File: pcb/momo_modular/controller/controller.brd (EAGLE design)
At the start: 19 parts, among them U6 PIC24F16KA101-X_PSSOP, U7 FLASH8MSOP8

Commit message: Finished version 1 of the controller and wall_power boards.
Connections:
- removed net RX: U6.6
- removed net TX: U6.11
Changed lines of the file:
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@@
 <text x="31.877" y="40.9194" size="0.8128" layer="21">D</text>
 <text x="31.877" y="39.624" size="0.8128" layer="21">A</text>
-<dimension x1="55.88" y1="12.1158" x2="55.88" y2="42.6974" x3="58.8264" y3="27.4066" textsize="0.8128" layer="49" dtype="vertical" unit="inch" visible="yes"/>
 <wire x1="30.4292" y1="42.6466" x2="55.8292" y2="42.6466" width="0.254" layer="21"/>
 <wire x1="30.4292" y1="42.6466" x2="30.4292" y2="12.1666" width="0.254" layer="21"/>
 <wire x1="30.4292" y1="12.1666" x2="55.8292" y2="12.1666" width="0.254" layer="21"/>
-<dimension x1="30.4292" y1="42.6466" x2="55.88" y2="42.6974" x3="43.1546" y3="44.5262" textsize="0.8128" layer="21" dtype="horizontal" unit="inch" visible="yes"/>
+<dimension x1="30.4292" y1="42.6466" x2="55.8292" y2="42.6466" x3="43.1292" y3="45.6946" textsize="1.778" layer="49" dtype="horizontal" unit="inch" visible="yes"/>
+<dimension x1="55.88" y1="42.6974" x2="55.88" y2="12.1158" x3="27.0764" y3="27.4066" textsize="1.778" layer="49" dtype="vertical" unit="inch" visible="yes"/>
 </plain>
 <attributes>
@@
 <wire x1="36.8142" y1="37.8364" x2="37.6174" y2="37.0332" width="0.3048" layer="1"/>
 </signal>
-<signal name="RX">
-<contactref element="U6" pad="6"/>
-</signal>
-<signal name="TX">
-<contactref element="U6" pad="11"/>
-</signal>
 <signal name="SDI">

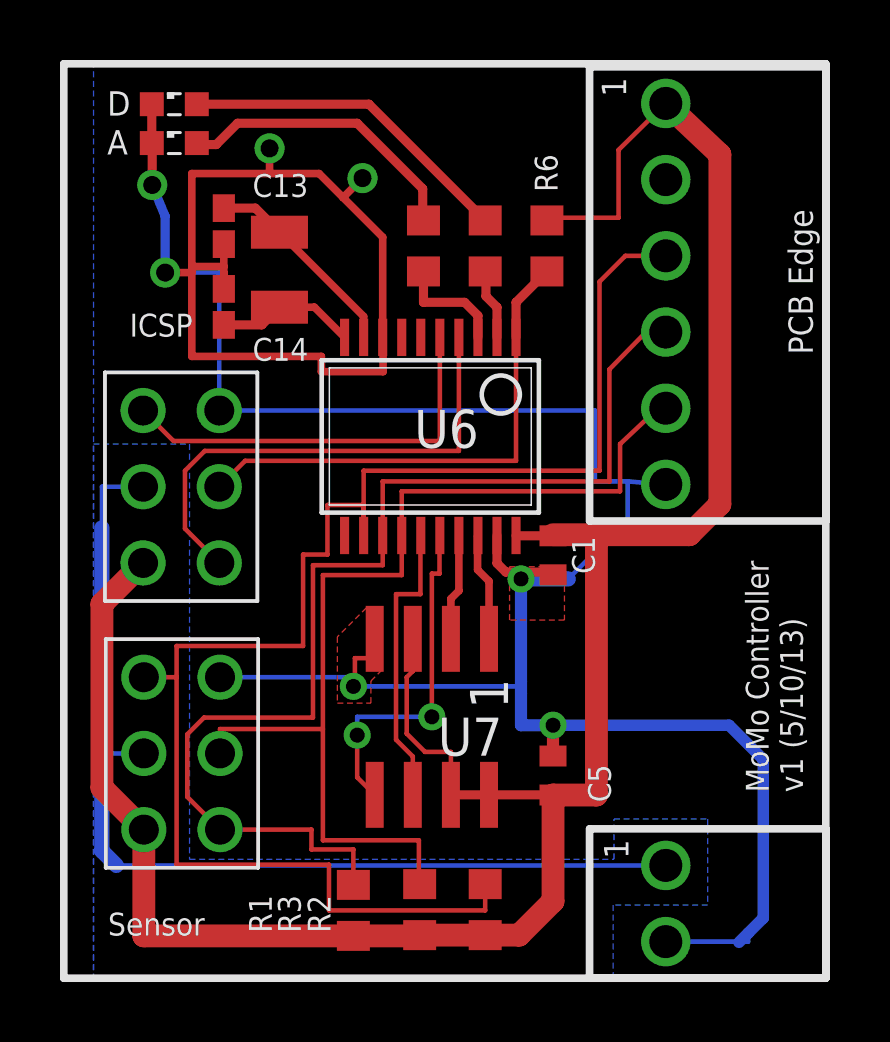
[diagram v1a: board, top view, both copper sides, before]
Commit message: Found better route without vias
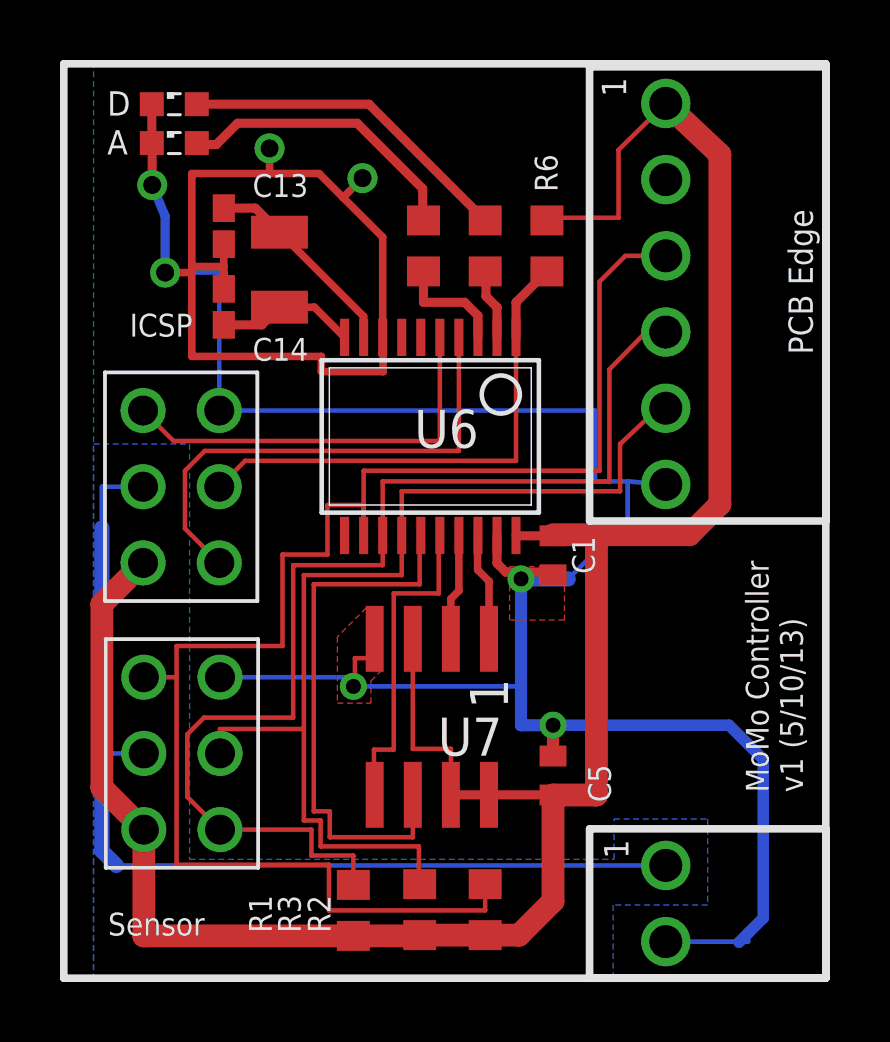
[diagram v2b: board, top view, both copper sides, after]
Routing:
- net SCLK: track 9.70 -> 18.3 mm
- net SDO: track 11.6 -> 10.9 mm, vias 2 -> 0
- net IRQ: track 34.0 -> 34.7 mm
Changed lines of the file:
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@@
 <contactref element="U$2" pad="1"/>
 <contactref element="U$3" pad="1"/>
-<wire x1="42.0624" y1="23.4788" x2="42.0624" y2="22.4028" width="0.1524" layer="1"/>
-<wire x1="42.0624" y1="22.4028" x2="41.8592" y2="22.1996" width="0.1524" layer="1"/>
-<wire x1="41.8592" y1="22.1996" x2="41.8592" y2="20.32" width="0.1524" layer="1"/>
-<wire x1="41.8592" y1="20.32" x2="42.4688" y2="19.7104" width="0.1524" layer="1"/>
-<wire x1="42.4688" y1="19.7104" x2="43.3324" y2="19.7104" width="0.1524" layer="1"/>
-<wire x1="43.3324" y1="19.7104" x2="43.3324" y2="18.2788" width="0.1524" layer="1"/>
 <wire x1="42.2656" y1="13.5772" x2="42.291" y2="13.6026" width="0.4064" layer="1"/>
 <wire x1="44.4754" y1="13.6026" x2="42.291" y2="13.6026" width="0.762" layer="1"/>
@@
 <wire x1="44.4754" y1="13.6026" x2="45.6066" y2="13.6026" width="0.762" layer="1"/>
 <wire x1="45.6066" y1="13.6026" x2="46.736" y2="14.732" width="0.762" layer="1"/>
+<wire x1="42.0624" y1="23.4788" x2="42.0624" y2="19.812" width="0.1524" layer="1"/>
+<wire x1="42.0624" y1="19.812" x2="43.3324" y2="19.812" width="0.1524" layer="1"/>
+<wire x1="43.3324" y1="19.812" x2="43.3324" y2="18.2788" width="0.1524" layer="1"/>
 </signal>
 <signal name="N$18">
@@
 <contactref element="U7" pad="6"/>
 <contactref element="U6" pad="15"/>
-<wire x1="42.3286" y1="26.924" x2="42.3164" y2="26.924" width="0.1524" layer="1"/>
-<wire x1="42.3164" y1="26.924" x2="42.3164" y2="24.9682" width="0.1524" layer="1"/>
-<wire x1="42.3164" y1="24.9682" x2="41.5036" y2="24.9682" width="0.1524" layer="1"/>
-<wire x1="41.5036" y1="24.9682" x2="41.5036" y2="20.1168" width="0.1524" layer="1"/>
-<wire x1="41.5036" y1="20.1168" x2="42.0624" y2="19.558" width="0.1524" layer="1"/>
-<wire x1="42.0624" y1="19.558" x2="42.0624" y2="18.2788" width="0.1524" layer="1"/>
+<wire x1="42.3286" y1="26.924" x2="42.291" y2="26.924" width="0.1524" layer="1"/>
+<wire x1="42.291" y1="26.924" x2="42.291" y2="25.2984" width="0.1524" layer="1"/>
+<wire x1="42.291" y1="25.2984" x2="38.7604" y2="25.2984" width="0.1524" layer="1"/>
+<wire x1="38.7604" y1="25.2984" x2="38.7604" y2="17.7292" width="0.1524" layer="1"/>
+<wire x1="38.7604" y1="17.7292" x2="39.2938" y2="17.7292" width="0.1524" layer="1"/>
+<wire x1="39.2938" y1="17.7292" x2="39.2938" y2="16.8656" width="0.1524" layer="1"/>
+<wire x1="39.2938" y1="16.8656" x2="42.0624" y2="16.8656" width="0.1524" layer="1"/>
+<wire x1="42.0624" y1="16.8656" x2="42.0624" y2="18.2788" width="0.1524" layer="1"/>
 </signal>
 <signal name="SDO">
 <contactref element="U6" pad="16"/>
 <contactref element="U7" pad="5"/>
-<wire x1="42.9636" y1="26.924" x2="42.9514" y2="26.924" width="0.1524" layer="1"/>
-<wire x1="42.9514" y1="26.924" x2="42.9514" y2="25.654" width="0.1524" layer="1"/>
-<wire x1="42.9514" y1="25.654" x2="42.6974" y2="25.654" width="0.1524" layer="1"/>
-<wire x1="42.6974" y1="25.654" x2="42.6974" y2="20.8788" width="0.1524" layer="1"/>
-<via x="42.6974" y="20.8788" extent="1-16" drill="0.5"/>
-<wire x1="42.6974" y1="20.8788" x2="40.2082" y2="20.8788" width="0.1524" layer="16"/>
-<wire x1="40.2082" y1="20.8788" x2="40.2082" y2="20.2692" width="0.1524" layer="16"/>
-<via x="40.2082" y="20.2692" extent="1-16" drill="0.5"/>
-<wire x1="40.2082" y1="20.2692" x2="40.2082" y2="18.863" width="0.1524" layer="1"/>
-<wire x1="40.2082" y1="18.863" x2="40.7924" y2="18.2788" width="0.1524" layer="1"/>
+<wire x1="42.9636" y1="26.924" x2="42.926" y2="26.924" width="0.1524" layer="1"/>
+<wire x1="42.926" y1="26.924" x2="42.926" y2="24.9936" width="0.1524" layer="1"/>
+<wire x1="42.926" y1="24.9936" x2="41.4274" y2="24.9936" width="0.1524" layer="1"/>
+<wire x1="41.4274" y1="24.9936" x2="41.4274" y2="19.7866" width="0.1524" layer="1"/>
+<wire x1="41.4274" y1="19.7866" x2="40.767" y2="19.7866" width="0.1524" layer="1"/>
+<wire x1="40.767" y1="19.7866" x2="40.767" y2="18.2788" width="0.1524" layer="1"/>
+<wire x1="40.767" y1="18.2788" x2="40.7924" y2="18.2788" width="0.1524" layer="1"/>
 </signal>
 <signal name="N$24">
@@
 <contactref element="U$3" pad="5"/>
 <wire x1="41.6936" y1="26.924" x2="41.6936" y2="25.6032" width="0.1524" layer="1"/>
-<wire x1="41.6936" y1="25.6032" x2="39.0652" y2="25.6032" width="0.1524" layer="1"/>
-<wire x1="39.0652" y1="25.6032" x2="39.0652" y2="20.4724" width="0.1524" layer="1"/>
-<wire x1="39.0652" y1="20.4724" x2="39.0652" y2="16.764" width="0.1524" layer="1"/>
-<wire x1="39.0652" y1="16.764" x2="42.2656" y2="16.764" width="0.1524" layer="1"/>
-<wire x1="42.2656" y1="16.764" x2="42.2656" y2="15.3026" width="0.1524" layer="1"/>
+<wire x1="41.6936" y1="25.6032" x2="38.4302" y2="25.6032" width="0.1524" layer="1"/>
+<wire x1="38.4302" y1="25.6032" x2="38.4302" y2="20.4724" width="0.1524" layer="1"/>
+<wire x1="38.989" y1="16.5608" x2="42.2656" y2="16.5608" width="0.1524" layer="1"/>
+<wire x1="42.2656" y1="16.5608" x2="42.2656" y2="15.3026" width="0.1524" layer="1"/>
 <wire x1="42.2656" y1="15.3026" x2="42.291" y2="15.3026" width="0.1524" layer="1"/>
 <wire x1="35.6362" y1="19.6596" x2="35.6362" y2="20.4724" width="0.1524" layer="1"/>
-<wire x1="35.6362" y1="20.4724" x2="39.0652" y2="20.4724" width="0.1524" layer="1"/>
+<wire x1="35.6362" y1="20.4724" x2="38.4302" y2="20.4724" width="0.1524" layer="1"/>
 <wire x1="48.9712" y1="28.3972" x2="41.6936" y2="28.3972" width="0.1524" layer="1"/>
 <wire x1="41.6936" y1="28.3972" x2="41.6936" y2="26.924" width="0.1524" layer="1"/>
@@
 <wire x1="48.9712" y1="29.972" x2="50.2412" y2="31.1658" width="0.1524" layer="1"/>
 <wire x1="50.2412" y1="31.1658" x2="50.4952" y2="31.1658" width="0.1524" layer="1"/>
+<wire x1="38.4302" y1="20.4724" x2="38.4302" y2="17.4244" width="0.1524" layer="1"/>
+<wire x1="38.4302" y1="17.4244" x2="38.989" y2="17.4244" width="0.1524" layer="1"/>
+<wire x1="38.989" y1="17.4244" x2="38.989" y2="16.5608" width="0.1524" layer="1"/>
 </signal>
 <signal name="IDAT">
@@
 <contactref element="U$3" pad="4"/>
 <wire x1="41.0586" y1="26.924" x2="41.0586" y2="25.9334" width="0.1524" layer="1"/>
-<wire x1="41.0586" y1="25.9334" x2="38.735" y2="25.9334" width="0.1524" layer="1"/>
-<wire x1="38.735" y1="25.9334" x2="38.735" y2="20.8534" width="0.1524" layer="1"/>
-<wire x1="38.735" y1="20.8534" x2="35.1028" y2="20.8534" width="0.1524" layer="1"/>
+<wire x1="41.0586" y1="25.9334" x2="38.0746" y2="25.9334" width="0.1524" layer="1"/>
+<wire x1="38.0746" y1="25.9334" x2="38.0746" y2="20.8534" width="0.1524" layer="1"/>
+<wire x1="38.0746" y1="20.8534" x2="35.1028" y2="20.8534" width="0.1524" layer="1"/>
 <wire x1="35.1028" y1="20.8534" x2="34.544" y2="20.2946" width="0.1524" layer="1"/>
 <wire x1="34.544" y1="20.2946" x2="34.544" y2="18.2118" width="0.1524" layer="1"/>
 <wire x1="34.544" y1="18.2118" x2="35.6362" y2="17.1196" width="0.1524" layer="1"/>
 <wire x1="35.6362" y1="17.1196" x2="38.6842" y2="17.1196" width="0.1524" layer="1"/>
-<wire x1="38.6842" y1="17.1196" x2="38.6842" y2="16.4592" width="0.1524" layer="1"/>
-<wire x1="38.6842" y1="16.4592" x2="40.0812" y2="16.4592" width="0.1524" layer="1"/>
-<wire x1="40.0812" y1="16.4592" x2="40.0812" y2="15.2772" width="0.1524" layer="1"/>
+<wire x1="38.6842" y1="17.1196" x2="38.6842" y2="16.256" width="0.1524" layer="1"/>
+<wire x1="38.6842" y1="16.256" x2="40.0812" y2="16.256" width="0.1524" layer="1"/>
+<wire x1="40.0812" y1="16.256" x2="40.0812" y2="15.2772" width="0.1524" layer="1"/>
 <wire x1="48.6156" y1="28.7274" x2="41.0586" y2="28.7274" width="0.1524" layer="1"/>
 <wire x1="41.0586" y1="28.7274" x2="41.0586" y2="26.924" width="0.1524" layer="1"/>
@@
 <wire x1="40.4236" y1="27.94" x2="39.2176" y2="27.94" width="0.1524" layer="1"/>
 <wire x1="39.2176" y1="27.94" x2="39.2176" y2="26.289" width="0.1524" layer="1"/>
-<wire x1="39.2176" y1="26.289" x2="38.4048" y2="26.289" width="0.1524" layer="1"/>
-<wire x1="38.4048" y1="26.289" x2="38.4048" y2="23.241" width="0.1524" layer="1"/>
-<wire x1="38.4048" y1="23.241" x2="34.1884" y2="23.241" width="0.1524" layer="1"/>
+<wire x1="39.2176" y1="26.289" x2="37.719" y2="26.289" width="0.1524" layer="1"/>
+<wire x1="37.719" y1="26.289" x2="37.719" y2="23.241" width="0.1524" layer="1"/>
+<wire x1="37.719" y1="23.241" x2="34.1884" y2="23.241" width="0.1524" layer="1"/>
 <wire x1="44.4754" y1="15.3026" x2="44.4754" y2="14.4272" width="0.1524" layer="1"/>
 <wire x1="44.4754" y1="14.4272" x2="39.2684" y2="14.4272" width="0.1524" layer="1"/>

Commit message: Controller Board v2.1 Done
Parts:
- removed U$2: 2X3-MOLEX-90130, components:2X3-MOLEX-90130
- removed U$4: MOMO-EDGE-SMALL-F, components:MOMO-EDGE-SMALL-6F
- added JP1: (no value), pinhead:1X05
- U$1: value MOMO-EDGE-POWER-F -> MOMO-EDGE-8F; device components:MOMO-EDGE-SMALL-2F -> components:MOMO-EDGE-8F
- moved U$3 17.1 mm to (52.6, 17.1)
- moved U$1 16.6 mm to (49.5, 31.2), turned to 0 degrees
- moved LED2 9.47 mm to (43.6, 40.7), turned to 270 degrees
- moved LED1 7.42 mm to (41.5, 40.7), turned to 270 degrees
- moved C14 2.41 mm to (37.2, 36.5)
- moved XTAL1 2.41 mm to (39.1, 39.0)
- moved C13 2.27 mm to (37.2, 39.0)
- moved R4 1.59 mm to (41.5, 37.9)
- moved R5 1.59 mm to (43.6, 37.9)
- moved R6 1.59 mm to (45.6, 37.9)
- moved R2 1.27 mm to (43.3, 14.8), turned to 90 degrees
- moved R3 1.12 mm to (41.2, 14.8), turned to 90 degrees
- moved C5 0.98 mm to (45.8, 18.6)
- moved U7 0.98 mm to (41.8, 20.5)
- moved R1 0.97 mm to (39.2, 14.8), turned to 90 degrees
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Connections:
- removed net N$18: U$2.3, U6.5
- removed net N$19: U$2.4, U6.4
- removed net NC: U$4.2
- new net N$6: JP1.4, U6.4
- new net N$7: JP1.5, U6.5
- net GND: now also JP1.3, U$1.GND, U$1.PGND; no longer U$1.2, U$2.6, U$4.6
- net ICLK: now also U$1.CLK; no longer U$4.3
- net IDAT: now also U$1.DAT; no longer U$4.4
- net IRQ: now also U$1.ARLM; no longer U$4.5
- net N$15: now also JP1.1; no longer U$2.5
- net V+: now also U$1.V4.; no longer U$1.1, U$2.2
- net VCCINT: now also U$1.V28; no longer U$2.1, U$4.1
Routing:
- net V+: track 33.9 -> 11.1 mm
- net VCCINT: track 79.5 -> 57.8 mm
- net N$7: track 0.00 -> 17.5 mm, vias 0 -> 2
- net N$19: track 16.8 -> 0.00 mm
- net N$6: track 0.00 -> 16.3 mm, vias 0 -> 2
- net N$18: track 13.8 -> 0.00 mm
- net IRQ: track 34.7 -> 45.4 mm, vias 0 -> 1
- net N$1: track 11.2 -> 1.22 mm
- net N$2: track 9.82 -> 1.22 mm
- net IDAT: track 38.2 -> 45.7 mm, vias 0 -> 1
- net GND: track 105.6 -> 103.1 mm, vias 7 -> 5
- net ICLK: track 51.9 -> 53.7 mm, vias 0 -> 3
- net N$15: track 17.0 -> 15.4 mm
- net N$25: track 6.85 -> 8.45 mm
- net SCLK: track 18.3 -> 17.1 mm
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- removed copper zone on layer 16, net V+
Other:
- board outline added: 21.8 x 30.5 mm
- board text added: "Momo v2.1"
- board text removed: "ICSP"
- board text removed: "MoMo Controller v1 (5/10/13)"
- board text removed: "Sensor"

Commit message: Improved one trace to avoid 2 vias
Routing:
- net ICLK: track 53.7 -> 59.0 mm, vias 3 -> 1
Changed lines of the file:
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@@
 <wire x1="33.9852" y1="42.6466" x2="33.9852" y2="12.1666" width="0.254" layer="20"/>
 <wire x1="33.9852" y1="12.1666" x2="55.8292" y2="12.1666" width="0.254" layer="20"/>
-<dimension x1="34.2392" y1="42.6466" x2="55.88" y2="42.6974" x3="45.0596" y3="44.3992" textsize="1.778" layer="48" dtype="horizontal" unit="inch" precision="3" visible="yes"/>
-<dimension x1="34.2392" y1="12.1666" x2="34.29" y2="42.672" x3="32.5882" y3="27.4193" textsize="1.778" layer="48" dtype="vertical" unit="inch" precision="3" visible="yes"/>
 <text x="36.6268" y="13.3858" size="1.016" layer="21" rot="R90">Momo v2.1</text>
+<dimension x1="33.9852" y1="42.6466" x2="55.8292" y2="42.6466" x3="44.9072" y3="44.6532" textsize="1.6764" layer="49" dtype="horizontal" unit="inch" precision="3" visible="yes"/>
+<dimension x1="33.9852" y1="42.6466" x2="33.9852" y2="12.1666" x3="32.258" y3="27.4066" textsize="1.6764" layer="49" dtype="vertical" unit="inch" precision="3" visible="yes"/>
 </plain>
 <attributes>
@@
 <wire x1="43.2562" y1="13.9582" x2="43.2308" y2="13.9328" width="0.1524" layer="1"/>
 <wire x1="43.2308" y1="13.9328" x2="43.2308" y2="13.3096" width="0.1524" layer="1"/>
-<via x="52.2478" y="21.6662" extent="1-16" drill="0.5"/>
-<wire x1="52.2478" y1="21.6662" x2="50.4698" y2="21.6662" width="0.1524" layer="16"/>
 <wire x1="49.4792" y1="36.2966" x2="49.3014" y2="36.2966" width="0.1524" layer="16"/>
 <wire x1="49.3014" y1="36.2966" x2="47.1932" y2="34.1884" width="0.1524" layer="16"/>
@@
 <wire x1="43.2308" y1="13.3096" x2="50.4698" y2="13.3096" width="0.1524" layer="1"/>
 <wire x1="50.4698" y1="13.3096" x2="51.054" y2="13.8938" width="0.1524" layer="1"/>
-<wire x1="51.054" y1="13.8938" x2="51.054" y2="15.24" width="0.1524" layer="1"/>
-<wire x1="51.054" y1="15.24" x2="50.546" y2="15.748" width="0.1524" layer="1"/>
-<wire x1="50.546" y1="15.748" x2="49.911" y2="15.748" width="0.1524" layer="1"/>
 <wire x1="49.911" y1="15.748" x2="49.022" y2="16.637" width="0.1524" layer="1"/>
 <wire x1="49.022" y1="16.637" x2="49.022" y2="17.526" width="0.1524" layer="1"/>
 <wire x1="49.022" y1="17.526" x2="50.038" y2="18.542" width="0.1524" layer="1"/>
 <wire x1="50.038" y1="18.542" x2="50.038" y2="19.6596" width="0.1524" layer="1"/>
-<via x="50.4698" y="21.6662" extent="1-16" drill="0.5"/>
-<wire x1="50.4698" y1="21.6662" x2="50.038" y2="21.2344" width="0.1524" layer="1"/>
-<wire x1="50.038" y1="21.2344" x2="50.038" y2="19.6596" width="0.1524" layer="1"/>
 <wire x1="49.4792" y1="36.2966" x2="52.2478" y2="36.2966" width="0.1524" layer="1"/>
 <wire x1="52.2478" y1="36.2966" x2="52.2478" y2="21.6662" width="0.1524" layer="1"/>
+<wire x1="52.2478" y1="21.6662" x2="52.578" y2="21.6662" width="0.1524" layer="1"/>
+<wire x1="52.578" y1="21.6662" x2="53.975" y2="20.2692" width="0.1524" layer="1"/>
+<wire x1="53.975" y1="20.2692" x2="53.975" y2="19.1262" width="0.1524" layer="1"/>
+<wire x1="53.975" y1="19.1262" x2="53.213" y2="18.3642" width="0.1524" layer="1"/>
+<wire x1="51.054" y1="17.399" x2="51.054" y2="15.113" width="0.1524" layer="1"/>
+<wire x1="51.054" y1="15.113" x2="51.054" y2="13.8938" width="0.1524" layer="1"/>
+<wire x1="53.213" y1="18.3642" x2="52.0192" y2="18.3642" width="0.1524" layer="1"/>
+<wire x1="52.0192" y1="18.3642" x2="51.054" y2="17.399" width="0.1524" layer="1"/>
+<wire x1="49.911" y1="15.748" x2="50.419" y2="15.748" width="0.1524" layer="1"/>
+<wire x1="50.419" y1="15.748" x2="51.054" y2="15.113" width="0.1524" layer="1"/>
 </signal>
 <signal name="N$4">
